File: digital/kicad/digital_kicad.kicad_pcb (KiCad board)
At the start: 2 copper layers, 14 parts, among them Q1 2N3904, Q2 2N3904, Q4 2N3904, SW1 SW_SPST

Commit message: kicad + pcb scheme review
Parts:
- added J1: Barrel_Jack_Switch, Connector_BarrelJack:BarrelJack_Wuerth_6941xx301002, F.Cu at (105.7, 74.1)
- added J2: Screw_Terminal_01x02, TerminalBlock_Phoenix:TerminalBlock_Phoenix_MKDS-1,5-2-5.08_1x02_P5.08mm_Horizontal, F.Cu at (156.5, 90.5)
- added R7: 33k, Resistor_SMD:R_0805_2012Metric_Pad1.20x1.40mm_HandSolder, F.Cu at (155.5, 78.0)
- C1, C2, C3: footprint Capacitor_THT:C_Disc_D3.0mm_W1.6mm_P2.50mm -> Capacitor_SMD:C_0805_2012Metric_Pad1.18x1.45mm_HandSolder
- R1, R2, R3, R4, R5, R6: footprint Resistor_THT:R_Axial_DIN0204_L3.6mm_D1.6mm_P7.62mm_Horizontal -> Resistor_SMD:R_0805_2012Metric_Pad1.20x1.40mm_HandSolder
- moved A1 72.9 mm to (141.9, 37.2), turned to 180 degrees
- moved SW1 45.5 mm to (184.0, 83.5), turned to 0 degrees
- moved C1 43.7 mm to (190.5, 69.0), turned to 90 degrees
- moved R2 40.9 mm to (190.5, 76.0), turned to 90 degrees
- moved Q1 39.4 mm to (183.5, 58.5), turned to 90 degrees
- moved R1 37.9 mm to (177.0, 82.5), turned to -90 degrees
- moved R6 28.9 mm to (155.5, 59.0)
- moved R3 28.9 mm to (162.5, 59.0)
- moved R5 23.6 mm to (169.5, 67.5)
- moved Q2 23.3 mm to (183.5, 65.0), turned to 90 degrees
- moved C2 17.5 mm to (161.5, 68.5), turned to -90 degrees
- moved Q4 16.9 mm to (183.5, 71.5), turned to 90 degrees
- moved R4 16.3 mm to (166.5, 78.0)
- moved C3 9.28 mm to (154.5, 68.5), turned to -90 degrees
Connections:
- A1 pad D2: Net-(A1-D2_INT0) -> unconnected-(A1-D2_INT0-PadD2)
- A1 pad VIN: unconnected-(A1-PadVIN) -> /VDC
- R4 pad 2: Net-(A1-D2_INT0) -> Net-(J2-Pin_1)
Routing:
- net /VDC: track 0.00 -> 29.6 mm
- net GND: track 112.6 -> 83.8 mm, vias 0 -> 6
- net Net-(A1-D2_INT0): track 23.9 -> 0.00 mm
- net Net-(J2-Pin_1): track 0.00 -> 21.5 mm
- net +5V: track 46.7 -> 65.1 mm, vias 0 -> 6
- net Net-(Q2-B): track 6.05 -> 22.0 mm
- net inv. SW: track 17.1 -> 28.2 mm
- net SW: track 24.4 -> 13.5 mm
- net Net-(Q1-B): track 11.3 -> 22.0 mm
- net A: track 29.6 -> 19.2 mm
- net Net-(Q2-C): track 20.5 -> 21.1 mm
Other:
- board outline added: 100 x 100 mm

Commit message: changedbarrel jack footprint
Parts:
- J1: footprint Connector_BarrelJack:BarrelJack_Wuerth_6941xx301002 -> Connector_BarrelJack:BarrelJack_GCT_DCJ200-10-A_Horizontal
- moved J1 18.3 mm to (123.8, 76.5), turned to -90 degrees
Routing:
- net /VDC: track 29.6 -> 10.5 mm
- net GND: track 83.8 -> 79.2 mm
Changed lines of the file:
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@@
 		)
 	)
-	(footprint "Connector_BarrelJack:BarrelJack_Wuerth_6941xx301002"
-		(layer "F.Cu")
-		(at 105.65 74.1 90)
-		(descr "Wuerth electronics barrel jack connector (5.5mm outher diameter, inner diameter 2.05mm or 2.55mm depending on exact order number), See: http://katalog.we-online.de/em/datasheet/6941xx301002.pdf")
+	(footprint "Connector_BarrelJack:BarrelJack_GCT_DCJ200-10-A_Horizontal"
+		(layer "F.Cu")
+		(at 123.8 76.5 -90)
+		(descr "Barrel jack connector (5.5 mm outer diameter, 2.05 inner diameter ), https://gct.co/files/drawings/dcj200-10.pdf")
 		(tags "connector barrel jack")
 		(property "Reference" "J1"
@@
 		)
 		(property "Datasheet" ""
-			(at 0 0 90)
+			(at 0 0 270)
 			(unlocked yes)
 			(layer "F.Fab")
@@
 			)
 		)
-		(property "Description" "DC Barrel Jack with an internal switch"
-			(at 0 0 90)
+		(property "Description" ""
+			(at 0 0 270)
 			(unlocked yes)
 			(layer "F.Fab")
@@
 		(attr through_hole)
 		(fp_line
-			(start -3.2 -1.3)
-			(end -4.9 -1.3)
-			(stroke
-				(width 0.12)
-				(type solid)
-			)
-			(layer "F.SilkS")
-		)
-		(fp_line
-			(start -4.9 -1.3)
+			(start -4.6 13.8)
+			(end -4.6 -0.7)
+			(stroke
+				(width 0.12)
+				(type solid)
+			)
+			(layer "F.SilkS")
+		)
+		(fp_line
+			(start 4.6 13.8)
+			(end -4.6 13.8)
+			(stroke
+				(width 0.12)
+				(type solid)
+			)
+			(layer "F.SilkS")
+		)
+		(fp_line
+			(start 4.6 5.2)
+			(end 4.6 13.8)
+			(stroke
+				(width 0.12)
+				(type solid)
+			)
+			(layer "F.SilkS")
+		)
+		(fp_line
+			(start -4.6 -0.7)
+			(end -2.6 -0.7)
+			(stroke
+				(width 0.12)
+				(type solid)
+			)
+			(layer "F.SilkS")
+		)
+		(fp_line
+			(start 2.6 -0.7)
+			(end 4.6 -0.7)
+			(stroke
+				(width 0.12)
+				(type solid)
+			)
+			(layer "F.SilkS")
+		)
+		(fp_line
+			(start 4.6 -0.7)
+			(end 4.6 0.6)
+			(stroke
+				(width 0.12)
+				(type solid)
+			)
+			(layer "F.SilkS")
+		)
+		(fp_line
+			(start -4.9 -1)
 			(end -4.9 0.3)
 			(stroke
@@
 		)
 		(fp_line
-			(start 4.6 -1)
-			(end 4.6 0.8)
-			(stroke
-				(width 0.12)
-				(type solid)
-			)
-			(layer "F.SilkS")
-		)
-		(fp_line
-			(start 2.5 -1)
-			(end 4.6 -1)
-			(stroke
-				(width 0.12)
-				(type solid)
-			)
-			(layer "F.SilkS")
-		)
-		(fp_line
-			(start -4.6 -1)
-			(end -2.5 -1)
-			(stroke
-				(width 0.12)
-				(type solid)
-			)
-			(layer "F.SilkS")
-		)
-		(fp_line
-			(start 4.6 5.2)
-			(end 4.6 13.7)
-			(stroke
-				(width 0.12)
-				(type solid)
-			)
-			(layer "F.SilkS")
-		)
-		(fp_line
-			(start 4.6 13.7)
-			(end -4.6 13.7)
-			(stroke
-				(width 0.12)
-				(type solid)
-			)
-			(layer "F.SilkS")
-		)
-		(fp_line
-			(start -4.6 13.7)
-			(end -4.6 -1)
-			(stroke
-				(width 0.12)
-				(type solid)
-			)
-			(layer "F.SilkS")
-		)
-		(fp_line
-			(start 5 -1.4)
-			(end -5 -1.4)
-			(stroke
-				(width 0.05)
-				(type solid)
-			)
-			(layer "F.CrtYd")
-		)
-		(fp_line
-			(start -5 -1.4)
-			(end -5 14.1)
-			(stroke
-				(width 0.05)
-				(type solid)
-			)
-			(layer "F.CrtYd")
-		)
-		(fp_line
-			(start 6.2 0.5)
-			(end 5 0.5)
-			(stroke
-				(width 0.05)
-				(type solid)
-			)
-			(layer "F.CrtYd")
-		)
-		(fp_line
-			(start 6.2 0.5)
-			(end 6.2 5.5)
-			(stroke
-				(width 0.05)
-				(type solid)
-			)
-			(layer "F.CrtYd")
-		)
-		(fp_line
-			(start 5 0.5)
-			(end 5 -1.4)
-			(stroke
-				(width 0.05)
-				(type solid)
-			)
-			(layer "F.CrtYd")
-		)
-		(fp_line
-			(start 6.2 5.5)
+			(start -3.2 -1)
+			(end -4.9 -1)
+			(stroke
+				(width 0.12)
+				(type solid)
+			)
+			(layer "F.SilkS")
+		)
+		(fp_line
+			(start -5 14.2)
+			(end 5 14.2)
+			(stroke
+				(width 0.05)
+				(type solid)
+			)
+			(layer "F.CrtYd")
+		)
+		(fp_line
+			(start 5 14.2)
 			(end 5 5.5)
 			(stroke
@@
 		)
 		(fp_line
-			(start 5 14.1)
+			(start 6.3 5.5)
 			(end 5 5.5)
 			(stroke
@@
 		)
 		(fp_line
-			(start -5 14.1)
-			(end 5 14.1)
-			(stroke
-				(width 0.05)
-				(type solid)
-			)
-			(layer "F.CrtYd")
-		)
-		(fp_line
-			(start 4.5 -0.9)
-			(end -3.5 -0.9)
-			(stroke
-				(width 0.1)
-				(type solid)
-			)
-			(layer "F.Fab")
-		)
-		(fp_line
-			(start 4.5 -0.9)
-			(end 4.5 13.6)
-			(stroke
-				(width 0.1)
-				(type solid)
-			)
-			(layer "F.Fab")
-		)
-		(fp_line
-			(start -4.5 0.1)
-			(end -3.5 -0.9)
-			(stroke
-				(width 0.1)
-				(type solid)
-			)
-			(layer "F.Fab")
-		)
-		(fp_line
-			(start 4.5 13.6)
-			(end -4.5 13.6)
-			(stroke
-				(width 0.1)
-				(type solid)
-			)
-			(layer "F.Fab")
-		)
-		(fp_line
-			(start -4.5 13.6)
-			(end -4.5 0.1)
+			(start 5 0.3)
+			(end 5 -1.5)
+			(stroke
+				(width 0.05)
+				(type solid)
+			)
+			(layer "F.CrtYd")
+		)
+		(fp_line
+			(start 6.3 0.3)
+			(end 6.3 5.5)
+			(stroke
+				(width 0.05)
+				(type solid)
+			)
+			(layer "F.CrtYd")
+		)
+		(fp_line
+			(start 6.3 0.3)
+			(end 5 0.3)
+			(stroke
+				(width 0.05)
+				(type solid)
+			)
+			(layer "F.CrtYd")
+		)
+		(fp_line
+			(start -5 -1.5)
+			(end -5 14.2)
+			(stroke
+				(width 0.05)
+				(type solid)
+			)
+			(layer "F.CrtYd")
+		)
+		(fp_line
+			(start 5 -1.5)
+			(end -5 -1.5)
+			(stroke
+				(width 0.05)
+				(type solid)
+			)
+			(layer "F.CrtYd")
+		)
+		(fp_line
+			(start -4.5 13.7)
+			(end -4.5 0.4)
+			(stroke
+				(width 0.1)
+				(type solid)
+			)
+			(layer "F.Fab")
+		)
+		(fp_line
+			(start 4.5 13.7)
+			(end -4.5 13.7)
+			(stroke
+				(width 0.1)
+				(type solid)
+			)
+			(layer "F.Fab")
+		)
+		(fp_line
+			(start -4.5 0.4)
+			(end -3.5 -0.6)
+			(stroke
+				(width 0.1)
+				(type solid)
+			)
+			(layer "F.Fab")
+		)
+		(fp_line
+			(start 4.5 -0.6)
+			(end 4.5 13.7)
+			(stroke
+				(width 0.1)
+				(type solid)
+			)
+			(layer "F.Fab")
+		)
+		(fp_line
+			(start 4.5 -0.6)
+			(end -3.5 -0.6)
 			(stroke
 				(width 0.1)
@@
 		)
 		(fp_text user "${REFERENCE}"
-			(at 0 7.5 90)
+			(at 0 3 90)
 			(layer "F.Fab")
 			(effects
@@
 		)
 		(pad "1" thru_hole rect
-			(at 0 0 90)
-			(size 4.4 1.8)
-			(drill oval 3.4 0.8)
+			(at 0 0 270)
+			(size 4.6 2)
+			(drill oval 3.6 1)
 			(layers "*.Cu" "*.Mask")
 			(remove_unused_layers no)
@@
 		)
 		(pad "2" thru_hole oval
-			(at 0 5.8 90)
-			(size 4 1.8)
-			(drill oval 3 0.8)
+			(at 0 6.3 270)
+			(size 4.2 2)
+			(drill oval 3.2 1)
 			(layers "*.Cu" "*.Mask")
 			(remove_unused_layers no)
@@
 		)
 		(pad "3" thru_hole oval
-			(at 4.8 3 180)
-			(size 4 1.8)
-			(drill oval 3 0.8)
+			(at 4.8 2.9 270)
+			(size 2 4.2)
+			(drill oval 1 3.2)
 			(layers "*.Cu" "*.Mask")
 			(remove_unused_layers no)
@@
 		)
 		(embedded_fonts no)
-		(model "${KICAD9_3DMODEL_DIR}/Connector_BarrelJack.3dshapes/BarrelJack_Wuerth_6941xx301002.step"
+		(model "${KICAD9_3DMODEL_DIR}/Connector_BarrelJack.3dshapes/BarrelJack_GCT_DCJ200-10-A_Horizontal.step"
 			(offset
 				(xyz 0 0 0)
@@
 	)
 	(segment
-		(start 105.65 74.1)
-		(end 108.11 76.56)
+		(start 123.8 76.5)
+		(end 134.2 76.5)
 		(width 0.2)
 		(layer "F.Cu")
@@
 	)
 	(segment
-		(start 108.11 76.56)
+		(start 134.2 76.5)
 		(end 134.26 76.56)
 		(width 0.2)
@@
 	)
 	(segment
-		(start 108.65 69.3)
-		(end 108.65 71.3)
-		(width 0.2)
-		(layer "F.Cu")
-		(net 6)
-	)
-	(segment
-		(start 108.65 71.3)
-		(end 111.45 74.1)
+		(start 120.9 81.3)
+		(end 120.9 79.9)
+		(width 0.2)
+		(layer "F.Cu")
+		(net 6)
+	)
+	(segment
+		(start 120.101 73.899)
+		(end 134.139 73.899)
 		(width 0.2)
 		(layer "F.Cu")
@@
 	)
 	(segment
-		(start 111.45 74.1)
-		(end 134.18 74.1)
+		(start 120.9 79.9)
+		(end 117.5 76.5)
 		(width 0.2)
 		(layer "F.Cu")
@@
 		(width 0.2)
 		(layer "F.Cu")
+		(net 6)
+	)
+	(segment
+		(start 134.139 73.899)
+		(end 134.26 74.02)
+		(width 0.2)
+		(layer "F.Cu")
+		(net 6)
+	)
+	(segment
+		(start 117.5 76.5)
+		(end 120.101 73.899)
+		(width 0.2)
+		(layer "F.Cu")

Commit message: updated pcb with Jarek's changes
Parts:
- added D1: SMAJ13A, Diode_SMD:D_SMA, F.Cu at (128.0, 66.8)
- added D2: BZT52Bxx, Diode_SMD:D_SOD-123F, F.Cu at (139.3, 69.2)
- added D3: LED, LED_SMD:LED_0805_2012Metric_Pad1.15x1.40mm_HandSolder, F.Cu at (153.0, 69.8)
- added Q3: FDN340P, Package_TO_SOT_SMD:SOT-23, F.Cu at (134.0, 68.7)
- added R8: 33k, Resistor_SMD:R_0805_2012Metric_Pad1.20x1.40mm_HandSolder, F.Cu at (171.1, 69.8)
- added R9: 1k, Resistor_SMD:R_0805_2012Metric_Pad1.20x1.40mm_HandSolder, F.Cu at (152.0, 64.8)
- J1: footprint Connector_BarrelJack:BarrelJack_GCT_DCJ200-10-A_Horizontal -> Connector_BarrelJack:BarrelJack_Wuerth_6941xx301002
- R7: value 33k -> 100k
- moved A1 68.4 mm to (192.4, 83.4), turned to 90 degrees
- moved C1 35.4 mm to (160.2, 50.8), turned to 0 degrees
- moved R2 34.0 mm to (167.6, 50.8), turned to 180 degrees
- moved J2 32.4 mm to (180.6, 68.9), turned to 90 degrees
- moved Q1 28.9 mm to (154.7, 56.8), turned to 180 degrees
- moved SW1 28.0 mm to (174.1, 57.3), turned to 90 degrees
- moved Q2 23.3 mm to (161.7, 56.8), turned to 180 degrees
- moved R1 22.1 mm to (165.1, 63.8), turned to 90 degrees
- moved R7 21.9 mm to (134.0, 74.3)
- moved Q4 20.9 mm to (168.7, 56.8), turned to 180 degrees
- moved R4 14.9 mm to (171.1, 63.8), turned to -90 degrees
- moved C2 13.1 mm to (148.5, 69.3), turned to 90 degrees
- moved R6 12.0 mm to (160.6, 69.8), turned to -90 degrees
- moved C3 10.1 mm to (144.5, 69.3), turned to 90 degrees
- moved J1 7.83 mm to (122.5, 68.8)
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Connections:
- net Net-(Q2-C) renamed /OUT
- net SW renamed /SW
- net inv. SW renamed /inv. SW
- C2 pad 1: +5V -> Net-(D1-A1)
- C3 pad 1: +5V -> Net-(D1-A1)
- J1 pad 1: /VDC -> Net-(D1-A1)
- J2 pad 1: Net-(J2-Pin_1) -> /DIG_IN
- R4 pad 2: Net-(J2-Pin_1) -> /DIG_IN
- R7 pad 2: Net-(J2-Pin_1) -> Net-(D2-A)
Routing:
- net GND: track 79.2 -> 8.18 mm, vias 6 -> 2
- net +5V: track 65.1 -> 17.4 mm, vias 6 -> 0
- net Net-(D1-A1): track 0.00 -> 26.7 mm
- net Net-(J2-Pin_1): track 21.5 -> 0.00 mm
- net /VDC: track 10.5 -> 28.6 mm
- net Net-(Q2-B): track 22.0 -> 6.10 mm
- net /DIG_IN: track 0.00 -> 13.5 mm
- net /inv. SW: track 28.2 -> 15.9 mm
- net A: track 19.2 -> 7.57 mm, vias 0 -> 1
- net /SW: track 13.5 -> 23.3 mm
- net Net-(D2-A): track 0.00 -> 9.35 mm
- net /OUT: track 21.1 -> 27.1 mm, vias 0 -> 1
- net Net-(Q1-B): track 22.0 -> 17.7 mm
- net Net-(D3-K): track 0.00 -> 3.95 mm
- added copper zone on B.Cu, net GND
- added copper zone on F.Cu, net GND

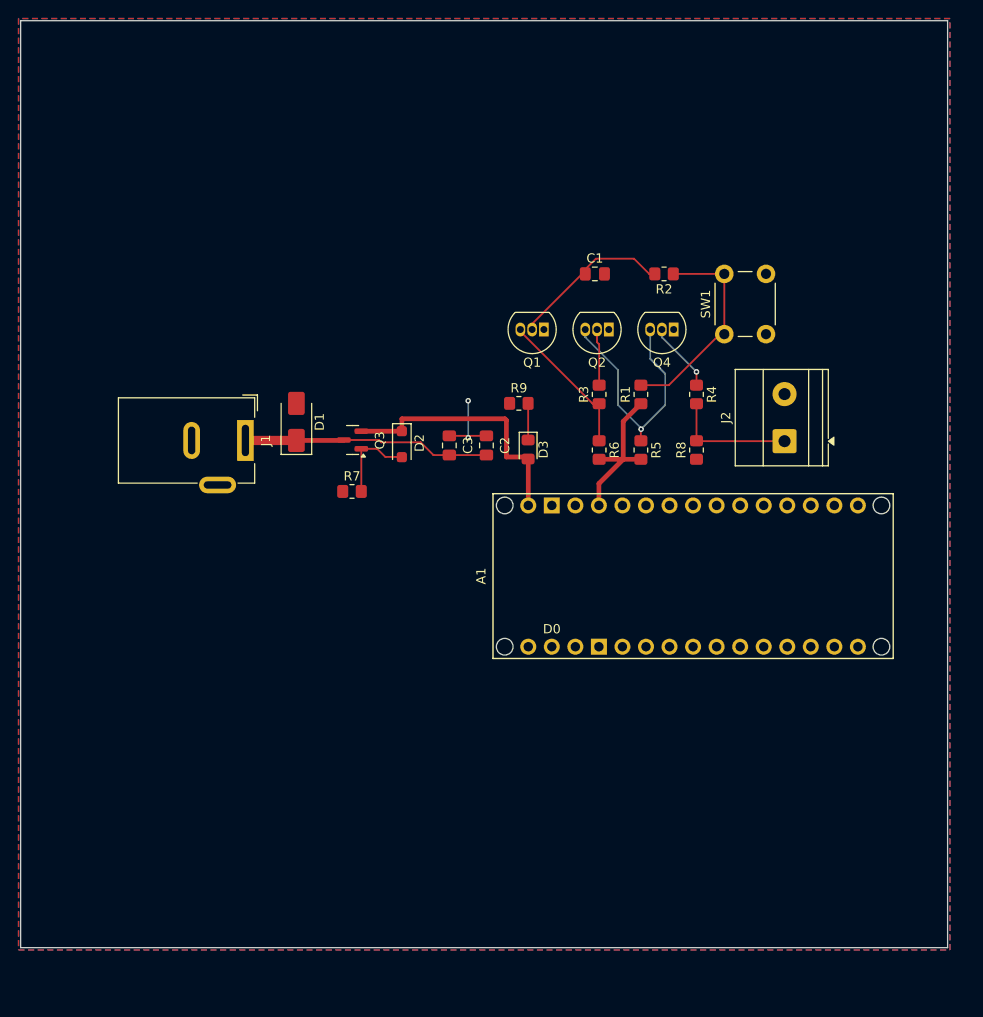
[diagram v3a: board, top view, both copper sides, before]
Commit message: reduced pcb board size to fit and increased vias to 05/08
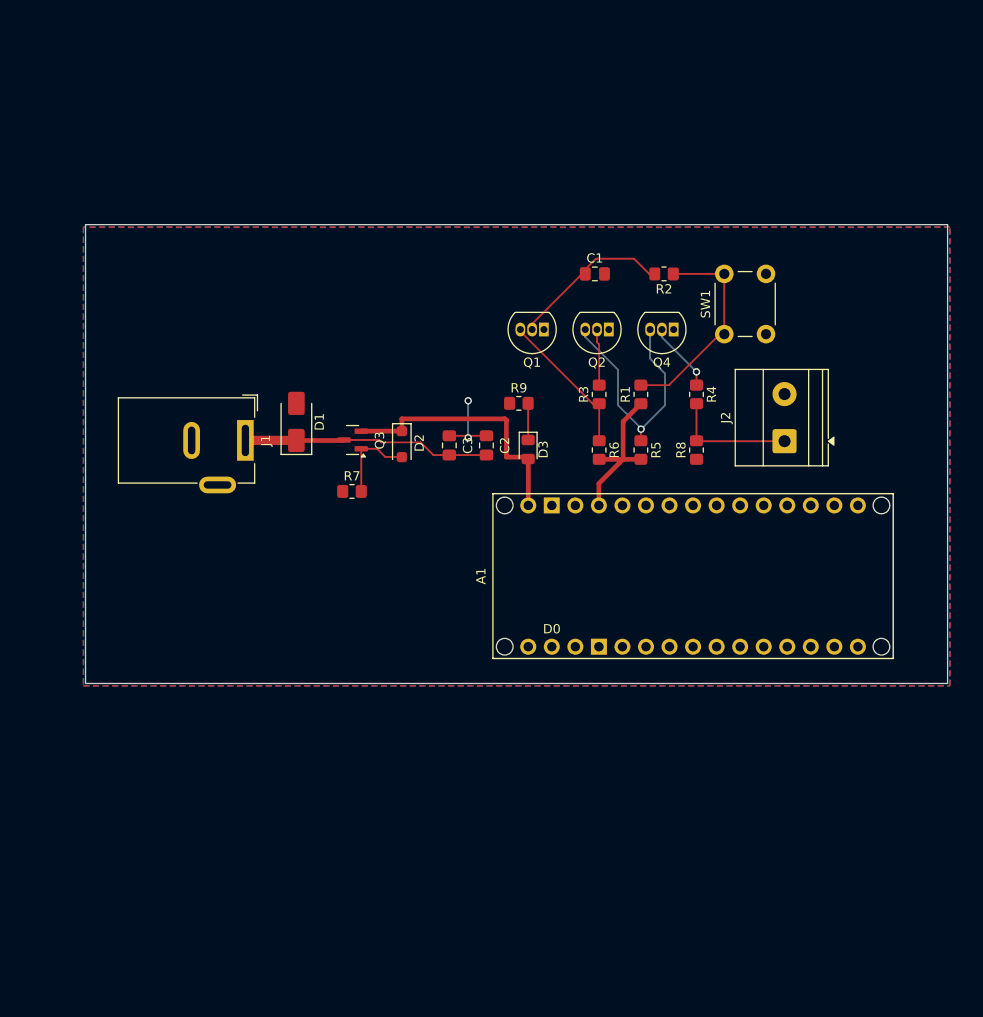
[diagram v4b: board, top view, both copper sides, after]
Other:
- board size 100 x 100 mm -> 93 x 49.5 mm
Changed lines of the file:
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@@
 			(outputformat 1)
 			(mirror no)
-			(drillshape 1)
+			(drillshape 0)
 			(scaleselection 1)
-			(outputdirectory "")
+			(outputdirectory "digital_v1")
 		)
 	)
@@
 	)
 	(gr_rect
-		(start 98.22 23.5)
-		(end 198.22 123.5)
+		(start 105.22 45.5)
+		(end 198.22 95)
 		(stroke
 			(width 0.05)
@@
 		)
 		(fill no)
-		(locked yes)
 		(layer "Edge.Cuts")
 	)
@@
 	(via
 		(at 146.5 64.5)
-		(size 0.6)
-		(drill 0.3)
+		(size 0.8)
+		(drill 0.5)
 		(layers "F.Cu" "B.Cu")
 		(free yes)
@@
 	(via
 		(at 146.5 68.5)
-		(size 0.6)
-		(drill 0.3)
+		(size 0.8)
+		(drill 0.5)
 		(layers "F.Cu" "B.Cu")
 		(free yes)
@@
 		(net 30)
 	)
-	(segment
-		(start 171.1452 61.3664)
-		(end 171.1296 61.382)
-		(width 0.2)
-		(layer "F.Cu")
-		(net 30)
-	)
 	(via
 		(at 171.1296 61.382)
-		(size 0.6)
-		(drill 0.3)
+		(size 0.8)
+		(drill 0.5)
 		(layers "F.Cu" "B.Cu")
 		(net 30)
@@
 	)
 	(segment
-		(start 165.1508 67.564)
-		(end 165.2016 67.5132)
-		(width 0.2)
-		(layer "F.Cu")
-		(net 39)
-	)
-	(segment
 		(start 165.1296 67.5852)
 		(end 165.1508 67.564)
@@
 	(via
 		(at 165.1508 67.564)
-		(size 0.6)
-		(drill 0.3)
+		(size 0.8)
+		(drill 0.5)
 		(layers "F.Cu" "B.Cu")
 		(net 39)
@@
 		(polygon
 			(pts
-				(xy 97.9932 23.2664) (xy 97.9932 123.7488) (xy 198.4756 123.7488) (xy 198.4756 23.2664)
+				(xy 104.9932 45.7664) (xy 104.9932 95.2488) (xy 198.4756 95.2488) (xy 198.4756 45.7664)
 			)
 		)
